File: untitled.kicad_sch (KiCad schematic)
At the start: 11 parts, among them J3 AVR-ISP-6, J4 AVR-ISP-6, J5 AVR-ISP-6, M1 Motor_DC, Q1 NMOS, U3 ATmega328P-P, U4 ATmega328P-P, U5 ATmega328P-P

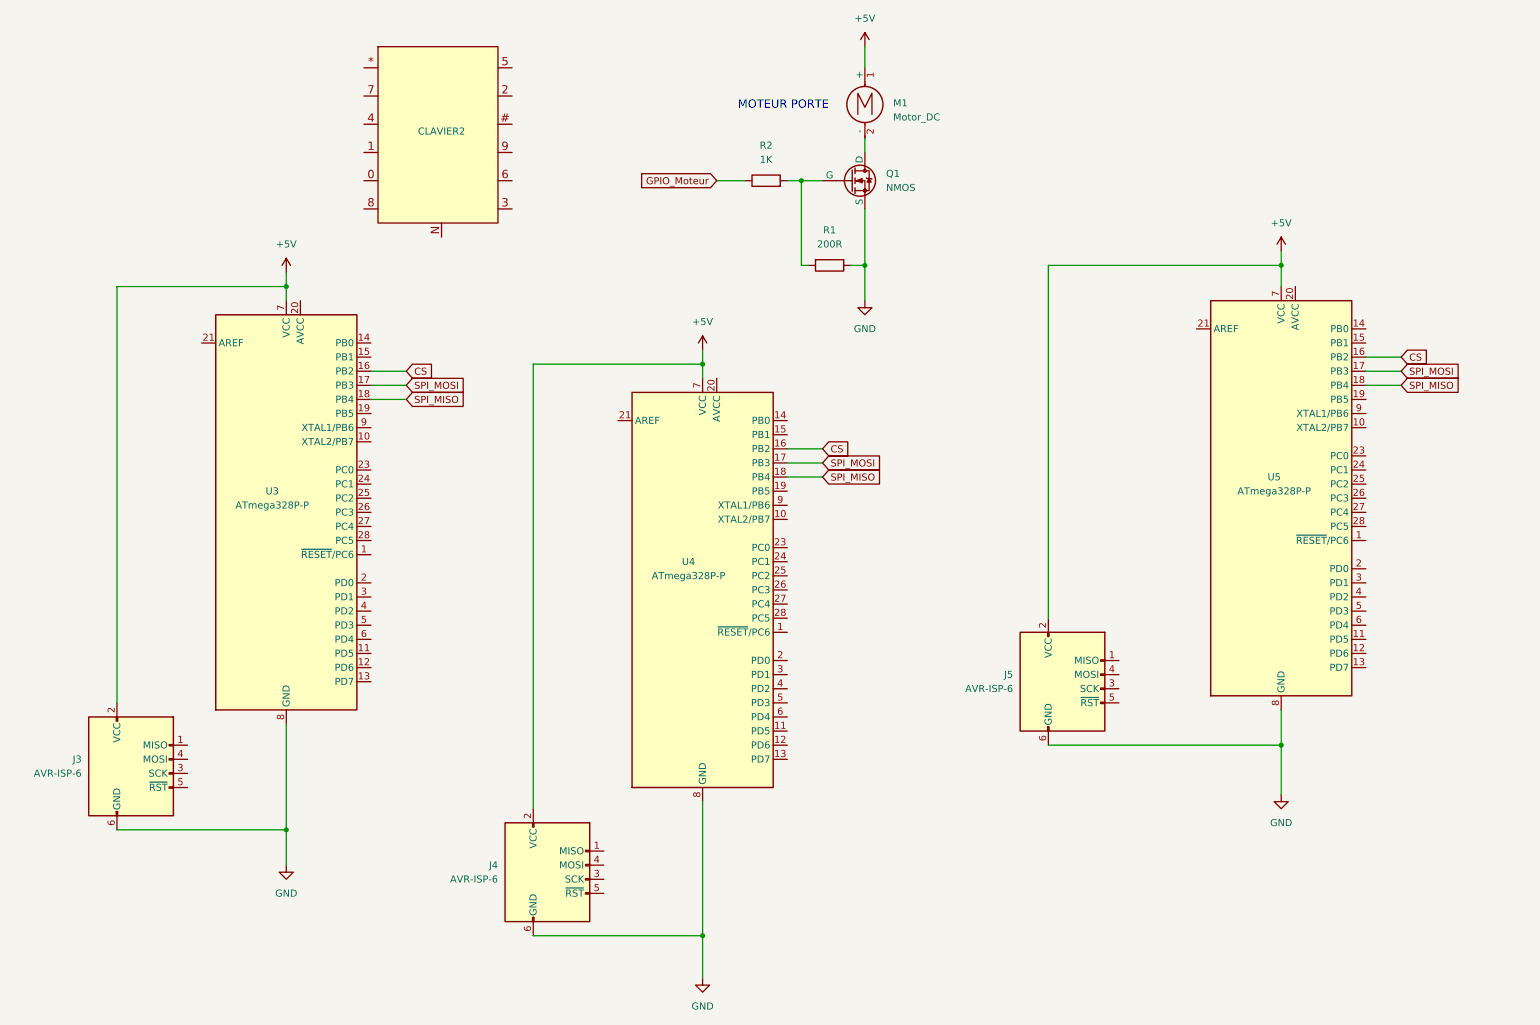
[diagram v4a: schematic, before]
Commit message: branchement du clavier
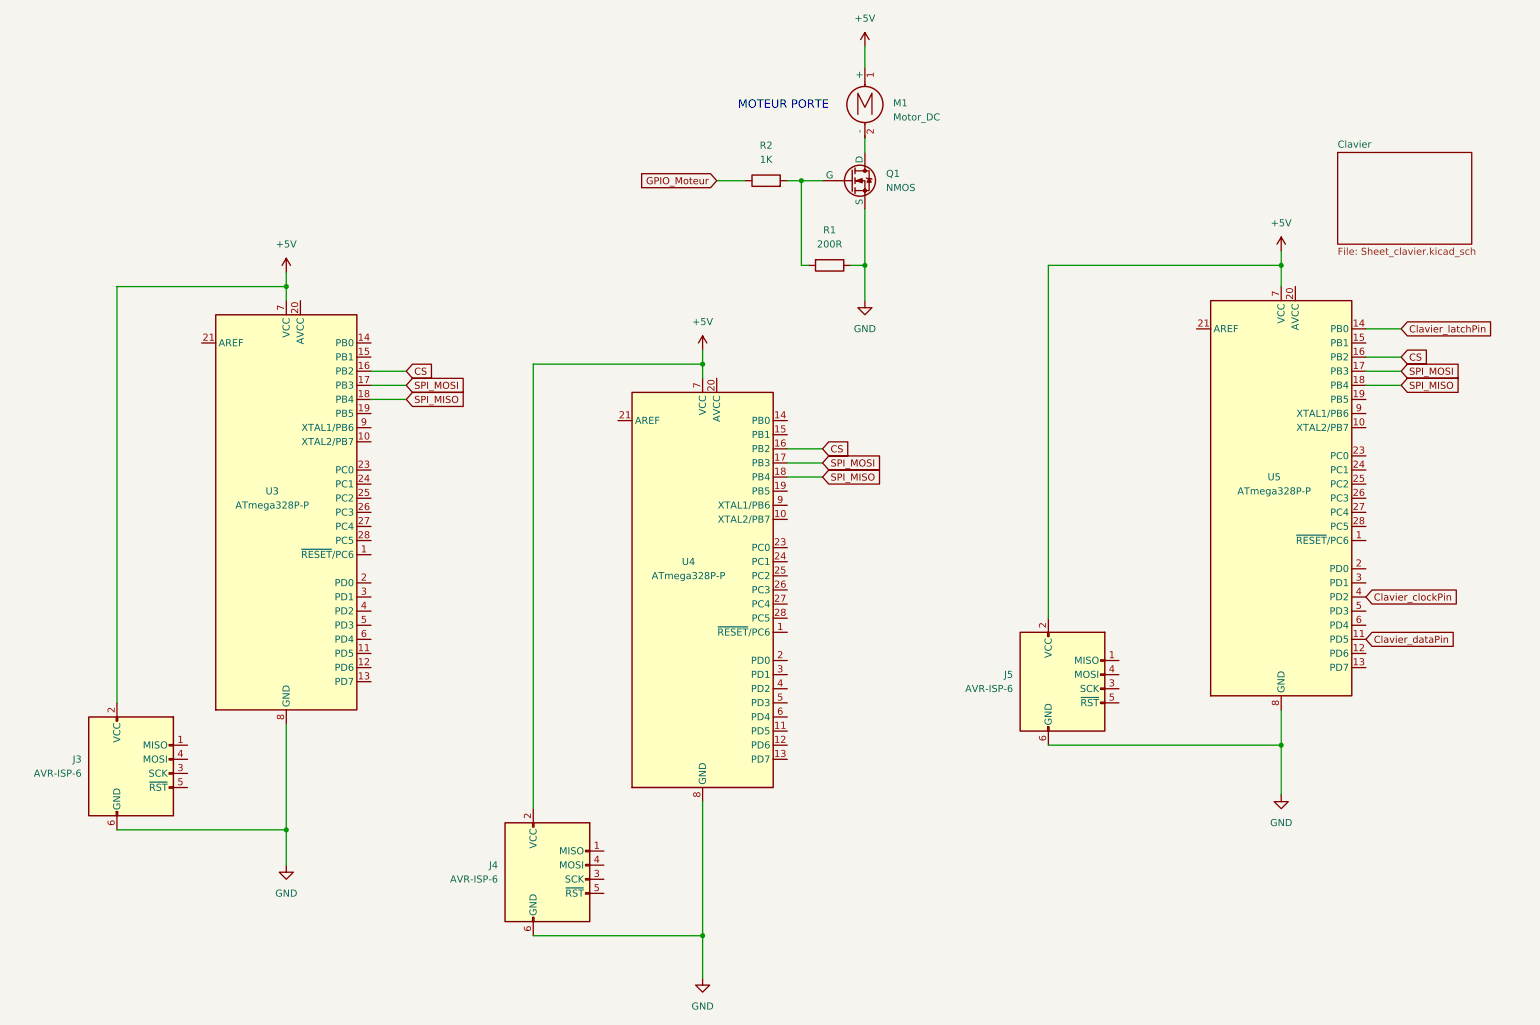
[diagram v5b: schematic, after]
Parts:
- removed CLAVIER2: ~, symbol New_Library:CLAV1
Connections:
- net Clavier_dataPin: now reaches U5.11 (PD5)
- net Clavier_latchPin: now reaches U5.14 (PB0)
- net Clavier_clockPin: now reaches U5.4 (PD2)
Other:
- added sheet Clavier (Sheet_clavier.kicad_sch)
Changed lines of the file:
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@@
+    (stroke (width 0) (type default))
+  )
+  (wire (pts (xy 255.27 73.66) (xy 261.62 73.66))
     (stroke (width 0) (type default))
   )
@@
     (effects (font (size 1.27 1.27)) (justify left))
     (property "Intersheetrefs" "${INTERSHEET_REFS}" (at 94.1039 86.36 0)
+      (effects (font (size 1.27 1.27)) (justify left) hide)
+    )
+  )
+  (global_label "Clavier_latchPin" (shape input) (at 261.62 73.66 0) (fields_autoplaced)
+    (effects (font (size 1.27 1.27)) (justify left))
+    (property "Intersheetrefs" "${INTERSHEET_REFS}" (at 279.8261 73.66 0)
       (effects (font (size 1.27 1.27)) (justify left) hide)
     )
@@
     )
   )
+  (global_label "Clavier_clockPin" (shape input) (at 255.27 121.92 0) (fields_autoplaced)
+    (effects (font (size 1.27 1.27)) (justify left))
+    (property "Intersheetrefs" "${INTERSHEET_REFS}" (at 273.7181 121.92 0)
+      (effects (font (size 1.27 1.27)) (justify left) hide)
+    )
+  )
   (global_label "CS" (shape input) (at 157.48 95.25 0) (fields_autoplaced)
     (effects (font (size 1.27 1.27)) (justify left))
@@
     (effects (font (size 1.27 1.27)) (justify left))
     (property "Intersheetrefs" "${INTERSHEET_REFS}" (at 267.0053 78.74 0)
+      (effects (font (size 1.27 1.27)) (justify left) hide)
+    )
+  )
+  (global_label "Clavier_dataPin" (shape input) (at 255.27 129.54 0) (fields_autoplaced)
+    (effects (font (size 1.27 1.27)) (justify left))
+    (property "Intersheetrefs" "${INTERSHEET_REFS}" (at 272.8713 129.54 0)
       (effects (font (size 1.27 1.27)) (justify left) hide)
     )
@@
     )
   )
-  (symbol (lib_name "CLAV1_1") (lib_id "New_Library:CLAV1") (at 88.9 38.1 0) (unit 1)
-    (in_bom yes) (on_board yes) (dnp no)
-    (property "Reference" "CLAVIER2" (at 88.9 38.1 0)
-      (effects (font (size 1.27 1.27)))
-    )
-    (property "Value" "~" (at 88.9 38.1 0)
-      (effects (font (size 1.27 1.27)))
-    )
-    (property "Footprint" "" (at 88.9 38.1 0)
-      (effects (font (size 1.27 1.27)) hide)
-    )
-    (property "Datasheet" "" (at 88.9 38.1 0)
-      (effects (font (size 1.27 1.27)) hide)
-    )
-    (pin "#")
-    (pin "*")
-    (pin "0")
-    (pin "1")
-    (pin "2")
-    (pin "3")
-    (pin "4")
-    (pin "5")
-    (pin "6")
-    (pin "7")
-    (pin "8")
-    (pin "9")
-    (pin "N")
-    (instances
-      (project "MaisonEtape1"
-        (path "/ed06f8de-d1bb-4b1a-bfe3-5df11d3a9162/0600536b-f413-4b06-98e9-b5748b5de992"
-          (reference "CLAVIER2") (unit 1)
-        )
-      )
-    )
-  )
   (symbol (lib_id "MCU_Microchip_ATmega:ATmega328P-P") (at 240.03 104.14 0) (unit 1)
     (in_bom yes) (on_board yes) (dnp no)
@@
       )
     )
+  )
+  (sheet (at 250.19 41.91) (size 24.13 16.51) (fields_autoplaced)
+    (stroke (width 0.1524) (type solid))
+    (fill (color 0 0 0 0.0000))
+    (property "Sheetname" "Clavier" (at 250.19 41.1984 0)
+      (effects (font (size 1.27 1.27)) (justify left bottom))
+    )
+    (property "Sheetfile" "Sheet_clavier.kicad_sch" (at 250.19 59.0046 0)
+      (effects (font (size 1.27 1.27)) (justify left top))
+    )
+    (instances
+      (project "MaisonEtape1"
+        (path "/ed06f8de-d1bb-4b1a-bfe3-5df11d3a9162/0600536b-f413-4b06-98e9-b5748b5de992" (page "4"))
+      )
+    )
